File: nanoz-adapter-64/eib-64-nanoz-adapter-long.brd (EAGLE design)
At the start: 24 x 89.5 mm, 4 parts, among them J1 DF40-REC, J4 SCREW2

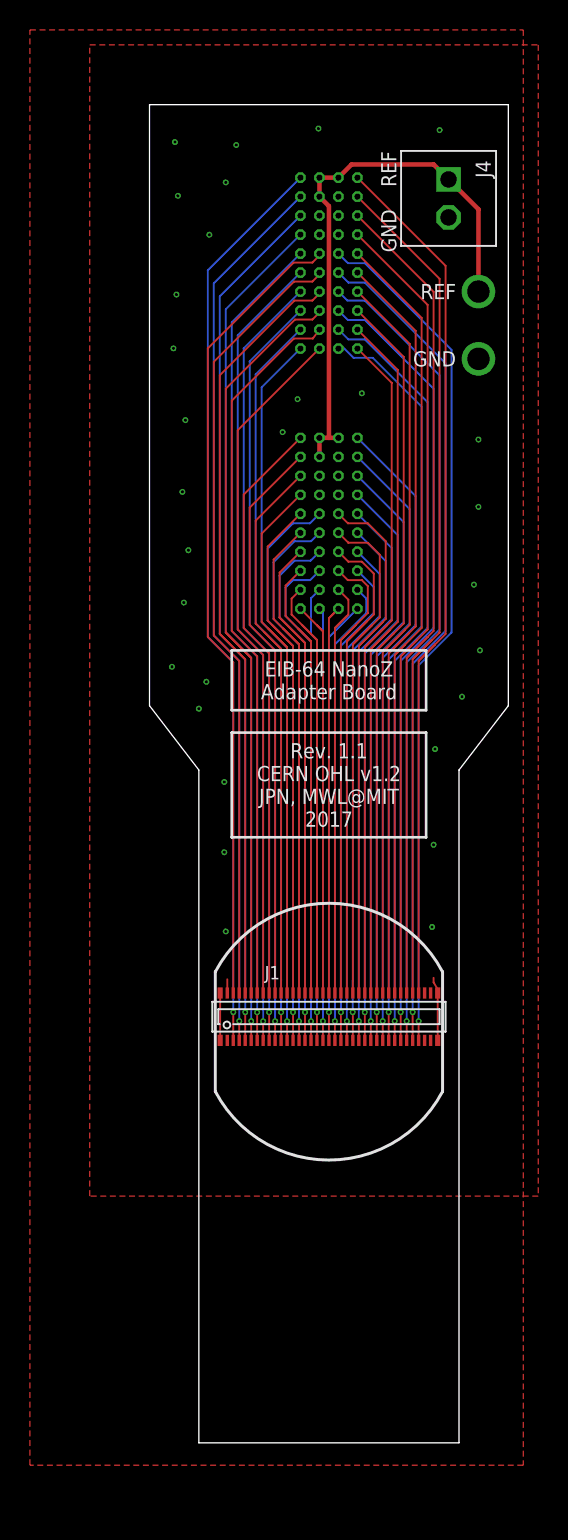
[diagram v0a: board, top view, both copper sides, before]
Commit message: updated long board to have top and bottom gnd planes
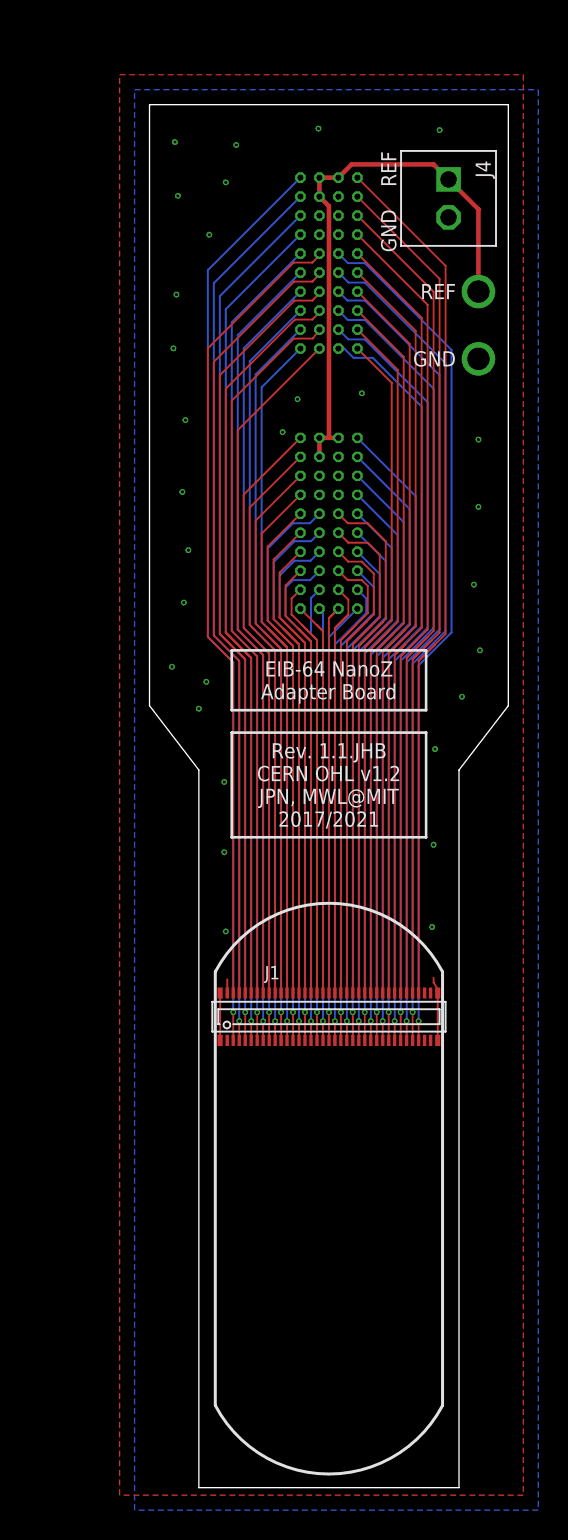
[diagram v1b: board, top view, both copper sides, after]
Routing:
- added copper zone on layer 16, net GND
- removed copper zone on layer 15, net GND
- removed copper zone on layer 2, net GND
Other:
- board size 24 x 89.5 mm -> 24 x 92.5 mm
- board text added: "Rev. 1.1.JHB CERN OHL v1.2 JPN, MWL@MIT 2017/2021"
- board text removed: "Rev. 1.1 CERN OHL v1.2 JPN, MWL@MIT 2017"
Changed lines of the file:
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@@
 <text x="0" y="47.5" size="1.016" layer="21" font="vector" ratio="19" align="center">EIB-64 NanoZ
 Adapter Board</text>
-<text x="0" y="40.5" size="1.016" layer="21" font="vector" ratio="19" align="center">Rev. 1.1
+<text x="0" y="40.5" size="1.016" layer="21" font="vector" ratio="19" align="center">Rev. 1.1.JHB
 CERN OHL v1.2
 JPN, MWL@MIT
-2017</text>
-<wire x1="8.7" y1="-3.5" x2="8.7" y2="41.5" width="0" layer="20"/>
+2017/2021</text>
+<wire x1="8.7" y1="-6.5" x2="8.7" y2="41.5" width="0" layer="20"/>
 <wire x1="11.99999375" y1="85.999965625" x2="-11.999996875" y2="85.999975" width="0" layer="20"/>
 <text x="8.5" y="69" size="1.016" layer="21" font="vector" ratio="18" align="center-right">GND</text>
@@
 <wire x1="-6.5" y1="44" x2="6.5" y2="44" width="0.1778" layer="21"/>
 <wire x1="6.5" y1="44" x2="6.5" y2="37" width="0.1778" layer="21"/>
-<wire x1="7.6" y1="20" x2="7.6" y2="28" width="0.2" layer="21"/>
-<wire x1="-7.6" y1="28" x2="-7.6" y2="20" width="0.2" layer="21"/>
+<wire x1="7.6" y1="-1" x2="7.6" y2="28" width="0.2" layer="21"/>
+<wire x1="-7.6" y1="28" x2="-7.6" y2="-1" width="0.2" layer="21"/>
 <wire x1="7.6" y1="28" x2="-7.6" y2="28" width="0.2" layer="21" curve="124.482919"/>
-<wire x1="7.6" y1="20" x2="-7.6" y2="20" width="0.2" layer="21" curve="-124.482919"/>
+<wire x1="7.6" y1="-1" x2="-7.6" y2="-1" width="0.2" layer="21" curve="-124.482919"/>
 <text x="4" y="79" size="1.016" layer="21" font="vector" ratio="18" rot="R90" align="center-right">GND</text>
 <text x="4" y="80.5" size="1.016" layer="21" font="vector" ratio="18" rot="R270" align="center-right">REF</text>
-<wire x1="-8.7" y1="41.5" x2="-8.7" y2="-3.5" width="0" layer="20"/>
+<wire x1="-8.7" y1="41.5" x2="-8.7" y2="-6.5" width="0" layer="20"/>
 <wire x1="-12" y1="45.8" x2="-12" y2="86" width="0" layer="20"/>
 <wire x1="12" y1="45.8" x2="12" y2="86" width="0" layer="20"/>
 <wire x1="-8.7" y1="41.5" x2="-12" y2="45.8" width="0" layer="20"/>
 <wire x1="8.7" y1="41.5" x2="12" y2="45.8" width="0" layer="20"/>
-<wire x1="8.7" y1="-3.5" x2="-8.7" y2="-3.5" width="0" layer="20"/>
+<wire x1="8.7" y1="-6.5" x2="-8.7" y2="-6.5" width="0" layer="20"/>
 </plain>
 <attributes>
@@
 <contactref element="J1" pad="M3"/>
 <contactref element="J4" pad="P$2"/>
-<polygon width="0.127" layer="1" rank="3">
-<vertex x="-15.999990625" y="89.99998125"/>
-<vertex x="13.99999375" y="89.999978125"/>
-<vertex x="13.999971875" y="13.000009375"/>
-<vertex x="-15.9999875" y="13.000021875"/>
-</polygon>
 <wire x1="-7.275" y1="23.415" x2="-7.275" y2="26.585" width="0.127" layer="1"/>
 <wire x1="7.275" y1="23.415" x2="7.275" y2="26.585" width="0.127" layer="1"/>
-<polygon width="0.127" layer="2" thermals="no" rank="3">
-<vertex x="-14.699990625" y="89.09998125"/>
-<vertex x="15.29999375" y="89.099978125"/>
-<vertex x="15.299971875" y="12.100009375"/>
-<vertex x="-14.6999875" y="12.100021875"/>
-</polygon>
-<polygon width="0.127" layer="15" thermals="no" rank="3">
-<vertex x="-17.399990625" y="90.89998125"/>
-<vertex x="12.59999375" y="90.899978125"/>
-<vertex x="12.599971875" y="13.900009375"/>
-<vertex x="-17.3999875" y="13.900021875"/>
-</polygon>
 <via x="8.9" y="46.4" extent="1-16" drill="0.2"/>
 <via x="10.1" y="49.5" extent="1-16" drill="0.2"/>
@@
 <via x="-7" y="36" extent="1-16" drill="0.2"/>
 <contactref element="J1" pad="37"/>
-<polygon width="0.1524" layer="1" isolate="0.254">
-<vertex x="-20" y="91"/>
-<vertex x="13" y="91"/>
-<vertex x="13" y="-5"/>
-<vertex x="-20" y="-5"/>
+<polygon width="0.1524" layer="1">
+<vertex x="-14" y="88"/>
+<vertex x="13" y="88"/>
+<vertex x="13" y="-7"/>
+<vertex x="-14" y="-7"/>
+</polygon>
+<polygon width="0.1524" layer="16">
+<vertex x="-13" y="87"/>
+<vertex x="14" y="87"/>
+<vertex x="14" y="-8"/>
+<vertex x="-13" y="-8"/>
 </polygon>
 </signal>
